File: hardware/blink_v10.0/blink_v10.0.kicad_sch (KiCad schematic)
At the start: 132 parts, among them J1 Conn_01x02, J14 Conn_02x16_Odd_Even, J15 Conn_01x01, J16 Conn_01x01, J5 Conn_01x06_Pin, J6 Conn_01x03, J7 Conn_01x06_Pin, J9 USB_C_Receptacle, Q1 S8550, Q2 S8050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

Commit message: Fixes #211 led setting when not running
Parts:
- added R? (x3): 47K, Resistor_SMD:R_0603_1608Metric, symbol Device:R_Small_US
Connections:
- net +3.3V: now also R?.2
- net GND: now also R?.1, R?.1
- net LEDMG: now also R?.2
- net LEDMR: now also R?.1
- net LEDMY: now also R?.2
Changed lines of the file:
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@@
   (junction (at 111.76 30.48) (diameter 0) (color 0 0 0 0)
   )
+  (junction (at 109.22 130.81) (diameter 0) (color 0 0 0 0)
+  )
   (junction (at 100.33 180.34) (diameter 0) (color 0 0 0 0)
   )
   (junction (at 267.97 185.42) (diameter 0) (color 0 0 0 0)
   )
+  (junction (at 100.33 125.73) (diameter 0) (color 0 0 0 0)
+  )
   (junction (at 68.58 88.9) (diameter 0) (color 0 0 0 0)
   )
@@
   (junction (at 142.24 252.73) (diameter 0) (color 0 0 0 0)
   )
+  (junction (at 99.06 105.41) (diameter 0) (color 0 0 0 0)
+  )
   (junction (at 212.09 147.32) (diameter 0) (color 0 0 0 0)
   )
   (junction (at 255.27 200.66) (diameter 0) (color 0 0 0 0)
   )
+  (junction (at 100.33 142.24) (diameter 0) (color 0 0 0 0)
+  )
   (junction (at 377.19 81.28) (diameter 0) (color 0 0 0 0)
   )
@@
   (junction (at 45.72 217.17) (diameter 0) (color 0 0 0 0)
   )
+  (junction (at 109.22 147.32) (diameter 0) (color 0 0 0 0)
+  )
   (junction (at 120.65 201.93) (diameter 0) (color 0 0 0 0)
   )
@@
     (stroke (width 0) (type default))
   )
+  (wire (pts (xy 100.33 130.81) (xy 109.22 130.81))
+    (stroke (width 0) (type default))
+  )
   (wire (pts (xy 92.71 63.5) (xy 100.33 63.5))
     (stroke (width 0) (type default))
@@
     (stroke (width 0) (type default))
   )
+  (wire (pts (xy 99.06 102.87) (xy 99.06 105.41))
+    (stroke (width 0) (type default))
+  )
   (wire (pts (xy 54.61 201.93) (xy 78.74 201.93))
     (stroke (width 0) (type default))
@@
     (stroke (width 0) (type default))
   )
-  (wire (pts (xy 95.25 142.24) (xy 101.6 142.24))
+  (wire (pts (xy 95.25 142.24) (xy 100.33 142.24))
     (stroke (width 0) (type default))
   )
@@
     (stroke (width 0) (type default))
   )
+  (wire (pts (xy 99.06 105.41) (xy 101.6 105.41))
+    (stroke (width 0) (type default))
+  )
   (wire (pts (xy 228.6 212.09) (xy 228.6 213.36))
     (stroke (width 0) (type default))
@@
     (stroke (width 0) (type default))
   )
+  (wire (pts (xy 100.33 125.73) (xy 101.6 125.73))
+    (stroke (width 0) (type default))
+  )
   (wire (pts (xy 140.97 201.93) (xy 140.97 193.04))
     (stroke (width 0) (type default))
@@
     (stroke (width 0) (type default))
   )
+  (wire (pts (xy 100.33 142.24) (xy 101.6 142.24))
+    (stroke (width 0) (type default))
+  )
   (wire (pts (xy 124.46 21.59) (xy 124.46 24.13))
     (stroke (width 0) (type default))
@@
     (stroke (width 0) (type default))
   )
+  (wire (pts (xy 100.33 147.32) (xy 109.22 147.32))
+    (stroke (width 0) (type default))
+  )
   (wire (pts (xy 111.76 21.59) (xy 111.76 24.13))
     (stroke (width 0) (type default))
@@
     (stroke (width 0) (type default))
   )
+  (wire (pts (xy 95.25 105.41) (xy 99.06 105.41))
+    (stroke (width 0) (type default))
+  )
   (wire (pts (xy 189.23 88.9) (xy 185.42 88.9))
     (stroke (width 0) (type default))
@@
     (stroke (width 0) (type default))
   )
+  (wire (pts (xy 95.25 125.73) (xy 100.33 125.73))
+    (stroke (width 0) (type default))
+  )
   (text "I2C Addr: 0x48 (7bit)" (at 289.56 22.86 0)
     (effects (font (size 1.27 1.27)) (justify left bottom))
@@
     (effects (font (size 1.27 1.27)) (justify right bottom))
   )
-  (label "LEDMG" (at 101.6 125.73 180) (fields_autoplaced)
+  (label "LEDMG" (at 95.25 125.73 180) (fields_autoplaced)
     (effects (font (size 1.27 1.27)) (justify right bottom))
   )
@@
     (effects (font (size 1.27 1.27)) (justify left bottom))
   )
-  (label "LEDMR" (at 101.6 105.41 180) (fields_autoplaced)
+  (label "LEDMR" (at 95.25 105.41 180) (fields_autoplaced)
     (effects (font (size 1.27 1.27)) (justify right bottom))
   )
@@
     (effects (font (size 1.27 1.27)) (justify right bottom))
   )
-  (label "LEDMY" (at 95.25 142.24 0) (fields_autoplaced)
-    (effects (font (size 1.27 1.27)) (justify left bottom))
+  (label "LEDMY" (at 95.25 142.24 180) (fields_autoplaced)
+    (effects (font (size 1.27 1.27)) (justify right bottom))
   )
   (label "SWDIO" (at 135.89 76.2 0) (fields_autoplaced)
@@
     )
   )
+  (symbol (lib_id "Device:R_Small_US") (at 99.06 100.33 180) (unit 1)
+    (in_bom yes) (on_board yes) (dnp no) (fields_autoplaced)
+    (property "Reference" "R?" (at 101.6 99.06 0)
+      (effects (font (size 1.27 1.27)) (justify right))
+    )
+    (property "Value" "47K" (at 101.6 101.6 0)
+      (effects (font (size 1.27 1.27)) (justify right))
+    )
+    (property "Footprint" "Resistor_SMD:R_0603_1608Metric" (at 99.06 100.33 0)
+      (effects (font (size 1.27 1.27)) hide)
+    )
+    (property "Datasheet" "~" (at 99.06 100.33 0)
+      (effects (font (size 1.27 1.27)) hide)
+    )
+    (property "JLCPCB Part #" "C25819" (at 99.06 100.33 0)
+      (effects (font (size 1.27 1.27)) hide)
+    )
+    (pin "1")
+    (pin "2")
+    (instances
+      (project "audio_amp_r1"
+        (path "/65a2a7ad-257a-48a0-a706-3da4b4be7c88"
+          (reference "R?") (unit 1)
+        )
+      )
+      (project "blink_v10.0"
+        (path "/bd4d3b9a-07c1-4a53-9c94-2893f3e869d4"
+          (reference "R51") (unit 1)
+        )
+      )
+    )
+  )
   (symbol (lib_id "power:GND") (at 109.22 130.81 0) (unit 1)
     (in_bom yes) (on_board yes) (dnp no) (fields_autoplaced)
@@
     )
   )
+  (symbol (lib_id "power:+3.3V") (at 99.06 97.79 0) (unit 1)
+    (in_bom yes) (on_board yes) (dnp no) (fields_autoplaced)
+    (property "Reference" "#PWR096" (at 99.06 101.6 0)
+      (effects (font (size 1.27 1.27)) hide)
+    )
+    (property "Value" "+3.3V" (at 99.06 92.71 0)
+      (effects (font (size 1.27 1.27)))
+    )
+    (property "Footprint" "" (at 99.06 97.79 0)
+      (effects (font (size 1.27 1.27)) hide)
+    )
+    (property "Datasheet" "" (at 99.06 97.79 0)
+      (effects (font (size 1.27 1.27)) hide)
+    )
+    (pin "1")
+    (instances
+      (project "blink_v10.0"
+        (path "/bd4d3b9a-07c1-4a53-9c94-2893f3e869d4"
+          (reference "#PWR096") (unit 1)
+        )
+      )
+    )
+  )
   (symbol (lib_id "Connector_Generic:Conn_01x01") (at 172.72 167.64 180) (unit 1)
     (in_bom no) (on_board yes) (dnp yes) (fields_autoplaced)
@@
     )
   )
+  (symbol (lib_id "Device:R_Small_US") (at 100.33 144.78 180) (unit 1)
+    (in_bom yes) (on_board yes) (dnp no) (fields_autoplaced)
+    (property "Reference" "R?" (at 102.87 143.51 0)
+      (effects (font (size 1.27 1.27)) (justify right))
+    )
+    (property "Value" "47K" (at 102.87 146.05 0)
+      (effects (font (size 1.27 1.27)) (justify right))
+    )
+    (property "Footprint" "Resistor_SMD:R_0603_1608Metric" (at 100.33 144.78 0)
+      (effects (font (size 1.27 1.27)) hide)
+    )
+    (property "Datasheet" "~" (at 100.33 144.78 0)
+      (effects (font (size 1.27 1.27)) hide)
+    )
+    (property "JLCPCB Part #" "C25819" (at 100.33 144.78 0)
+      (effects (font (size 1.27 1.27)) hide)
+    )
+    (pin "1")
+    (pin "2")
+    (instances
+      (project "audio_amp_r1"
+        (path "/65a2a7ad-257a-48a0-a706-3da4b4be7c88"
+          (reference "R?") (unit 1)
+        )
+      )
+      (project "blink_v10.0"
+        (path "/bd4d3b9a-07c1-4a53-9c94-2893f3e869d4"
+          (reference "R53") (unit 1)
+        )
+      )
+    )
+  )
   (symbol (lib_id "74xGxx:SN74LVC1G14DBV") (at 243.84 245.11 0) (unit 1)
     (in_bom yes) (on_board yes) (dnp no)
@@
         )
       )
+    )
+  )
+  (symbol (lib_id "Device:R_Small_US") (at 100.33 128.27 180) (unit 1)
+    (in_bom yes) (on_board yes) (dnp no) (fields_autoplaced)
+    (property "Reference" "R?" (at 102.87 127 0)
+      (effects (font (size 1.27 1.27)) (justify right))
+    )
+    (property "Value" "47K" (at 102.87 129.54 0)
+      (effects (font (size 1.27 1.27)) (justify right))
+    )
+    (property "Footprint" "Resistor_SMD:R_0603_1608Metric" (at 100.33 128.27 0)
+      (effects (font (size 1.27 1.27)) hide)
+    )
+    (property "Datasheet" "~" (at 100.33 128.27 0)
+      (effects (font (size 1.27 1.27)) hide)
+    )
+    (property "JLCPCB Part #" "C25819" (at 100.33 128.27 0)
+      (effects (font (size 1.27 1.27)) hide)
+    )
+    (pin "1")
+    (pin "2")
+    (instances
+      (project "audio_amp_r1"
+        (path "/65a2a7ad-257a-48a0-a706-3da4b4be7c88"
+          (reference "R?") (unit 1)
+        )
+      )
+      (project "blink_v10.0"
+        (path "/bd4d3b9a-07c1-4a53-9c94-2893f3e869d4"
+          (reference "R52") (unit 1)
+        )
+      )

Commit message: clean up units
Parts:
- R21, R22: value 5k1 -> 5K1
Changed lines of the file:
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@@
       (effects (font (size 1.27 1.27)) (justify left))
     )
-    (property "Value" "5k1" (at 383.54 219.71 90)
+    (property "Value" "5K1" (at 383.54 219.71 90)
       (effects (font (size 1.27 1.27)) (justify left))
     )
@@
       (effects (font (size 1.27 1.27)) (justify left))
     )
-    (property "Value" "5k1" (at 382.27 214.63 90)
+    (property "Value" "5K1" (at 382.27 214.63 90)
       (effects (font (size 1.27 1.27)) (justify left))
     )

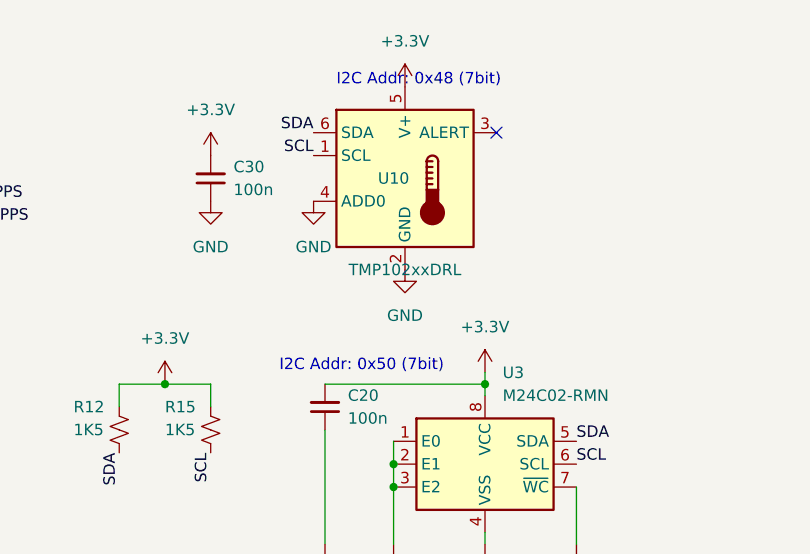
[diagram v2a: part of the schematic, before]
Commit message: change temp sensor to to TMP112A
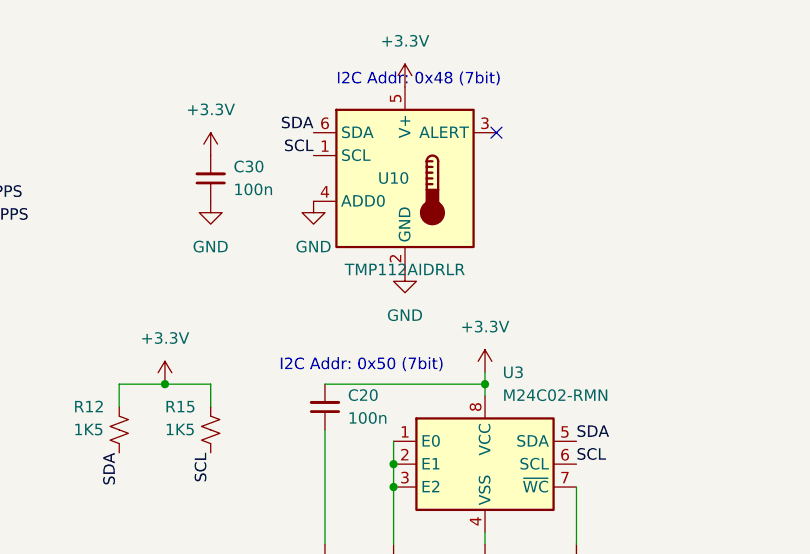
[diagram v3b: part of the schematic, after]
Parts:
- U10: value TMP102xxDRL -> TMP112AIDRLR; JLCPCB Part # C99269 -> C28927; JLCPCB Rotation Offset (none) -> 180
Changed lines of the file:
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@@
       (effects (font (size 1.27 1.27)))
     )
-    (property "Value" "TMP102xxDRL" (at 297.18 43.18 0)
+    (property "Value" "TMP112AIDRLR" (at 297.18 43.18 0)
       (effects (font (size 1.27 1.27)))
     )
@@
       (effects (font (size 1.27 1.27)) (justify left) hide)
     )
-    (property "JLCPCB Part #" "C99269" (at 297.18 33.02 0)
+    (property "JLCPCB Part #" "C28927" (at 297.18 33.02 0)
       (effects (font (size 1.27 1.27)) hide)
     )
+    (property "JLCPCB Rotation Offset" "180" (at 297.18 33.02 0)
+      (effects (font (size 1.27 1.27)) hide)
+    )

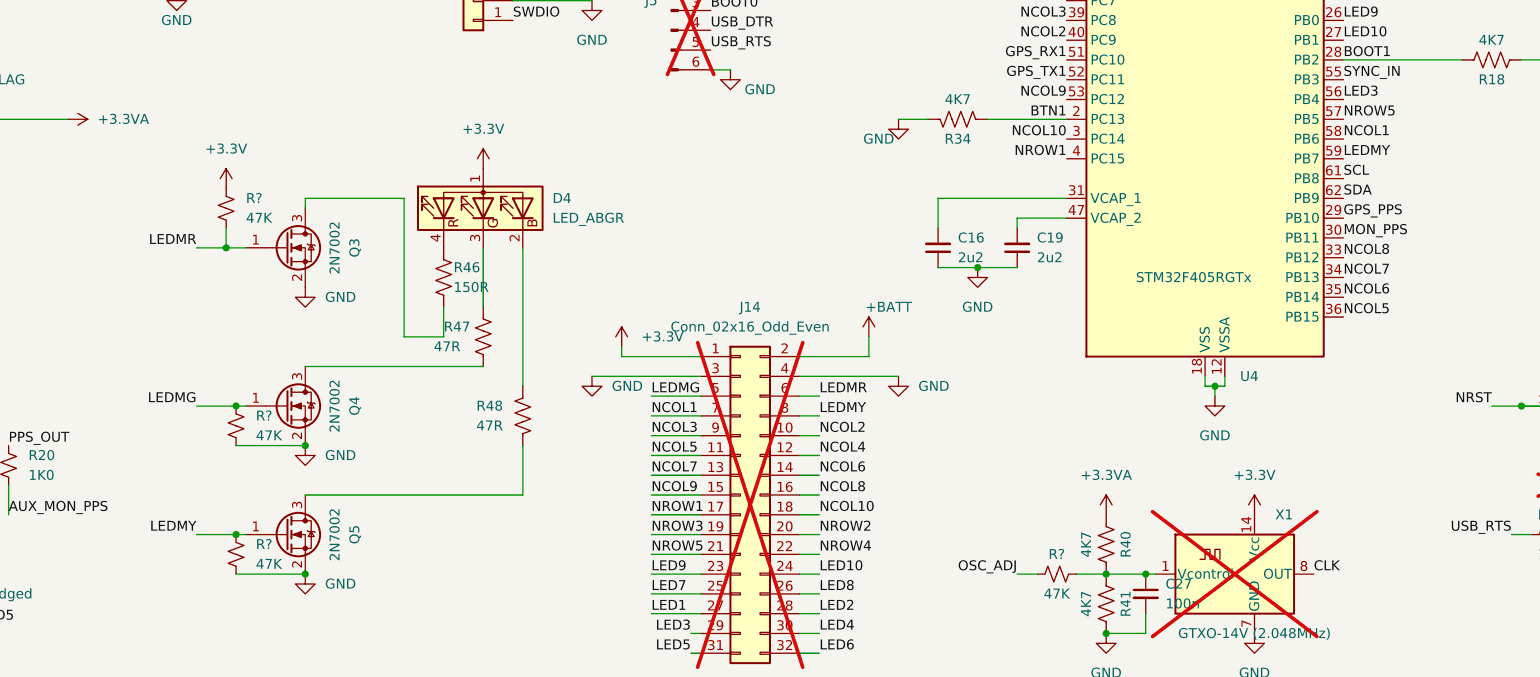
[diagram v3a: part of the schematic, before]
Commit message: change LEDMY to LEDMB. Fixes #230
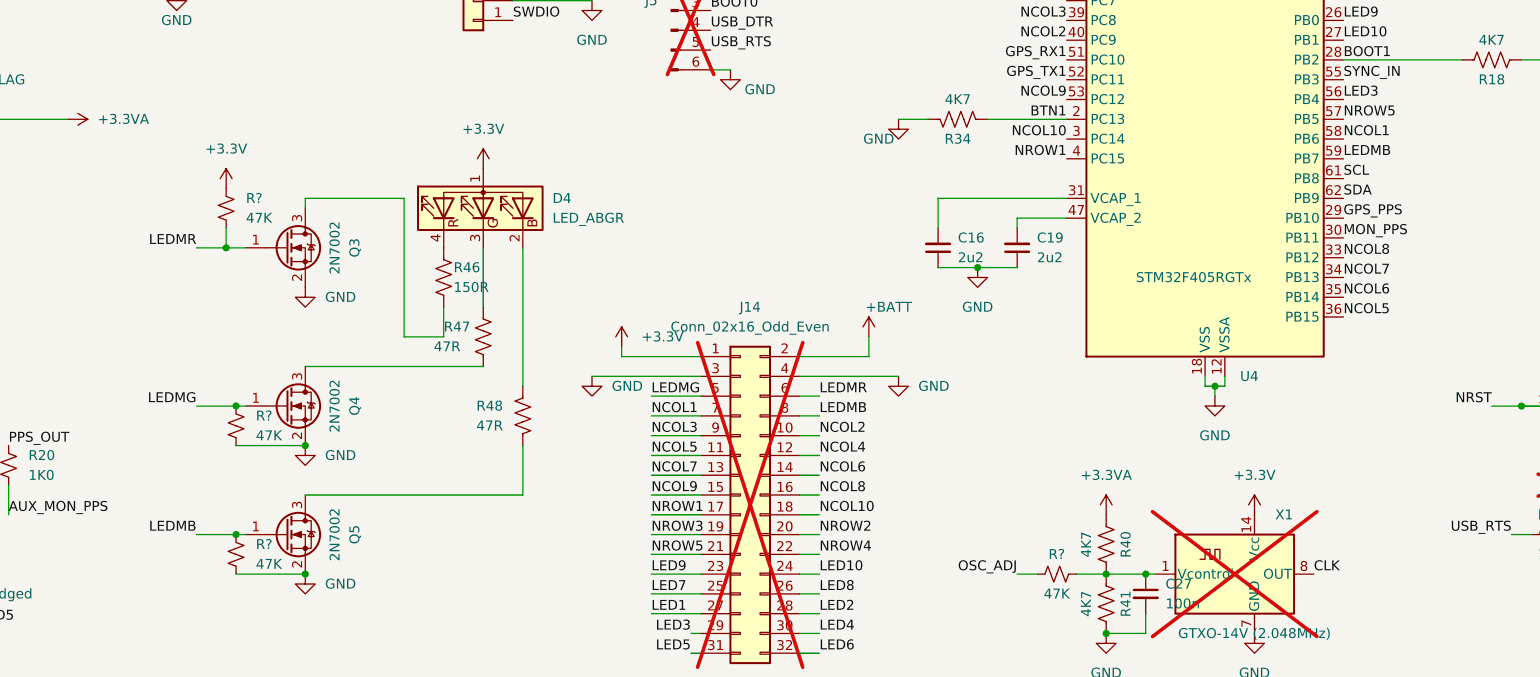
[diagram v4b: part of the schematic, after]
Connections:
- net LEDMY renamed LEDMB
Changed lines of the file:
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@@
     (effects (font (size 1.27 1.27)) (justify left bottom))
   )
-  (label "LEDMY" (at 175.26 127 0) (fields_autoplaced)
+  (label "LEDMB" (at 175.26 127 0) (fields_autoplaced)
     (effects (font (size 1.27 1.27)) (justify left bottom))
   )
@@
     (effects (font (size 1.27 1.27)) (justify right bottom))
   )
-  (label "LEDMY" (at 242.57 93.98 0) (fields_autoplaced)
+  (label "LEDMB" (at 242.57 93.98 0) (fields_autoplaced)
     (effects (font (size 1.27 1.27)) (justify left bottom))
   )
@@
     (effects (font (size 1.27 1.27)) (justify right bottom))
   )
-  (label "LEDMY" (at 95.25 142.24 180) (fields_autoplaced)
+  (label "LEDMB" (at 95.25 142.24 180) (fields_autoplaced)
     (effects (font (size 1.27 1.27)) (justify right bottom))
   )
